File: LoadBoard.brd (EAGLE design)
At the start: 100 x 100 mm, 76 parts, among them IC1 7805TV, IC2 LM358D, IC3 MCP23S17SO, Q1 IRFZ44N, Q2 16MHz, T1 BC817, U1 ATMEGA328P_TQFP, U2 MAX232SOIC16

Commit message: routed first version of the board
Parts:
- added ENCODER, JP3: (no value), SparkFun-Connectors:MOLEX-1X4
- added FAN_CTRL, VLOAD_ATT: TPB1,27, testpad:B1,27
- added H5, H6: 3MM, holes:3,0-PAD
- added KK3: SK104-PAD, heatsink:SK104-PAD
- added LED1, LED2: (no value), led:Q62902-B155
- added Q3: IRFZ44N, OwnStuff:TO-220-V
- added R14, R15, R16: 100, rcl:R1206
- added R17, R18: 4k7, rcl:M1206
- added RST_EN: (no value), pinhead:1X02
- added U$7, U$8: DS18B20, OwnStuff:TO-92
- KK1: value SK129 -> SK104-PAD; device heatsink:SK129-HOLE -> heatsink:SK104-PAD
- moved U$4 60.9 mm to (62.2, 38.1), turned to 270 degrees
- moved S1 58.3 mm to (41.9, 88.6)
- moved T1 54.3 mm to (62.2, 43.2), turned to 270 degrees
- moved R6 51.2 mm to (55.9, 43.2), turned to 0 degrees
- moved FAN 48.7 mm to (62.2, 47.0), turned to 90 degrees
- moved D1 45.4 mm to (55.9, 48.3), turned to 270 degrees
- moved KK1 44.9 mm to (91.4, 68.6), turned to 270 degrees
- moved Q1 38.4 mm to (86.4, 68.6), turned to 270 degrees
- moved R3 33.2 mm to (80.0, 72.4), turned to 0 degrees
- moved U$5 32.8 mm to (11.4, 48.3)
- moved R5 30.4 mm to (74.9, 48.9), turned to 90 degrees
- moved R13 30.2 mm to (80.0, 68.6), turned to 180 degrees
- moved Q2 28.0 mm to (41.9, 41.9)
- moved R12 27.9 mm to (80.0, 64.8), turned to 0 degrees
- moved C6 26.7 mm to (48.3, 48.3)
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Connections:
- new net GNDIO: JP3.1, S1.C, S1.SW-
- new net LED1: R14.1, U1.27
- new net LED2: R15.1, U1.28
- new net N$43: LED1.A, R14.2
- new net N$44: LED2.A, R15.2
- new net N$45: JP3.4, S1.SW+
- new net N$46: JP3.3, S1.A
- new net N$47: Q3.1, R16.2
- new net N$49: JP3.2, S1.B
- new net RST_EN: C12.2, RST_EN.1
- new net TH1: R18.2, U$7.2, U1.23
- new net TH2: R17.2, U$8.2, U1.24
- net +12V: now also FAN.2; no longer FAN.1
- net BTN_A: now also U1.2; no longer U1.1
- net BTN_B: now also U1.1; no longer U1.2
- net ENC_A: now also ENCODER.3; no longer S1.A
- net ENC_B: now also ENCODER.2; no longer S1.B
- net ENC_BTN: now also ENCODER.4; no longer S1.SW+
- net FAN: now also FAN_CTRL.TP
- net GND: now also ENCODER.1, LED1.K, LED2.K, U$7.1, U$8.1; no longer S1.C, S1.SW-
- net LOAD+: now also Q3.2
- net N$10: now also R16.1
- net N$12: now also DTR_IN.TP; no longer RX_IN.TP
- net N$13: now also RX_IN.TP; no longer DTR_IN.TP
- net N$26: now also PWR_SWITCH.2; no longer PWR_SWITCH.1
- net N$35: now also U$6.CS2; no longer U$6.DI
- net N$36: now also U$6.CS1; no longer U$6.RW
- net N$38: now also U$6.RW; no longer U$6.CS1
- net N$39: now also U$6.DI; no longer U$6.CS2
- net N$41: now also PWR_SWITCH.1; no longer PWR_SWITCH.2
- net N$5: now also FAN.1; no longer FAN.2
- net N$7: now also RST_EN.2; no longer C12.2
- net VCC: now also R17.1, R18.1, U$7.3, U$8.3
- net VLOAD_ATT: now also VLOAD_ATT.TP
- net VLOAD_DROP: now also Q3.3, U1.25
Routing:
- net VCC: track 0.00 -> 233.1 mm, vias 0 -> 7
- net VLOAD_DROP: track 0.00 -> 161.5 mm, vias 0 -> 1
- net +12V: track 0.00 -> 123.2 mm, vias 0 -> 2
- net TH1: track 0.00 -> 120.8 mm, vias 0 -> 3
- net TH2: track 0.00 -> 115.6 mm, vias 0 -> 2
- net MOSI: track 0.00 -> 107.8 mm, vias 0 -> 3
- net SCK: track 0.00 -> 97.2 mm, vias 0 -> 2
- net VLOAD_ATT: track 0.00 -> 95.8 mm, vias 0 -> 2
- net RST: track 0.00 -> 92.4 mm, vias 0 -> 2
- net BTN_B: track 0.00 -> 92.0 mm, vias 0 -> 2
- net LOAD+: track 0.00 -> 87.3 mm
- net BTN_A: track 0.00 -> 87.0 mm, vias 0 -> 2
- net LED1: track 0.00 -> 72.9 mm, vias 0 -> 2
- net N$10: track 0.00 -> 72.1 mm
- net CS1: track 0.00 -> 68.1 mm, vias 0 -> 2
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- added copper zone on layer 1, net GNDIO
- added copper zone on layer 16, net GNDIO
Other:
- board size 100 x 100 mm -> 99 x 99 mm

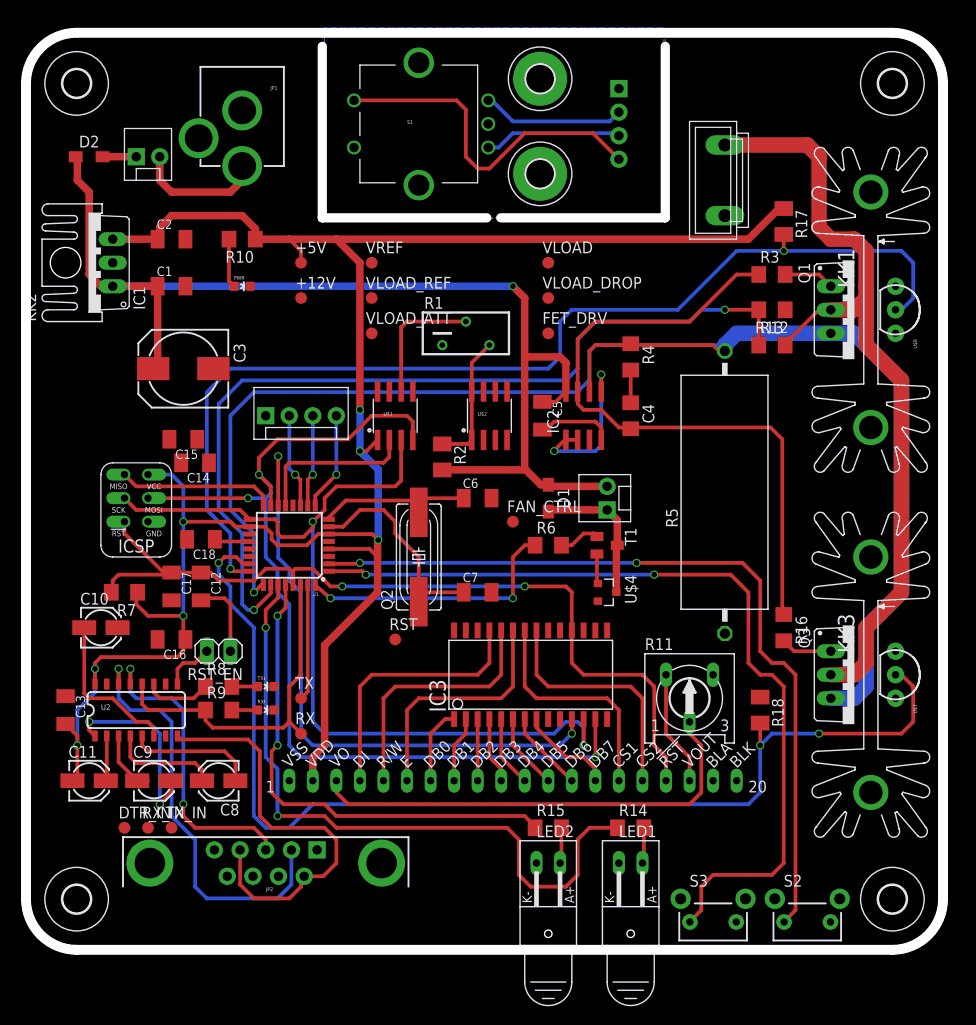
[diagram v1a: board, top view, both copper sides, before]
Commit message: Routed more of the Board, added an optional LM2569 Module
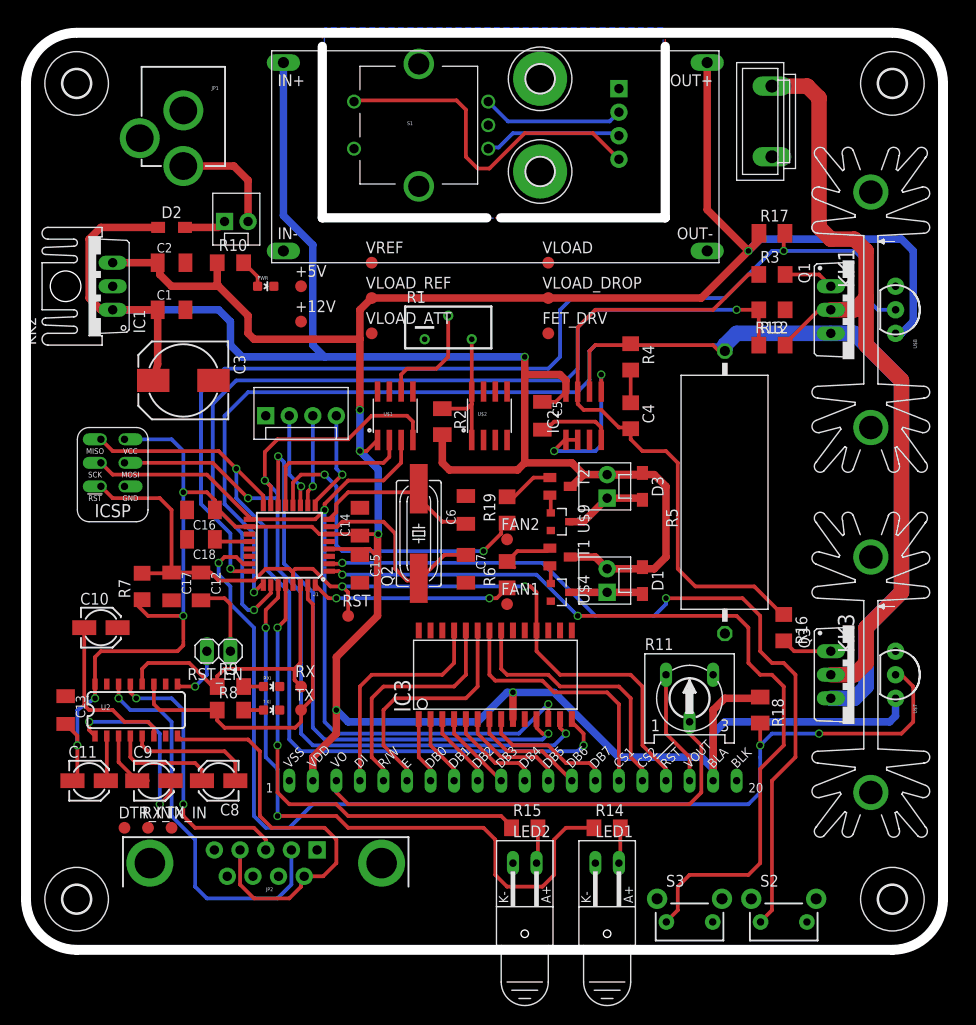
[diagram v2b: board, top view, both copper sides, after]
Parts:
- removed FAN: (no value), SparkFun-Connectors:MOLEX-1X2
- removed FAN_CTRL: TPB1,27, testpad:B1,27
- added D3: BAS16J, diode:SOD323-W
- added FAN1, FAN2: TPB1,27, testpad:B1,27
- added FAN1_CONN, FAN2_CONN: (no value), SparkFun-Connectors:MOLEX-1X2
- added R19: 100, rcl:R1206
- added T2: BC817, transistor:SOT23-BEC
- added U$10: LM2569, OwnStuff:LM2596
- added U$9: IRLML2502, GeekAmmo:SOT23-3
- moved C15 23.6 mm to (35.6, 40.6), turned to 270 degrees
- moved C14 18.9 mm to (35.6, 45.7), turned to 90 degrees
- moved C16 14.3 mm to (18.4, 47.0)
- moved D1 13.5 mm to (66.0, 39.4)
- moved PWR_SWITCH 11.8 mm to (21.0, 78.1)
- moved D2 11.7 mm to (15.2, 77.5)
- moved U$3 8.13 mm to (80.0, 88.9)
- moved JP1 6.35 mm to (16.5, 97.8)
- moved RST 5.68 mm to (34.3, 35.6)
- moved R6 5.46 mm to (51.4, 40.0), turned to 90 degrees
- moved T1 5.24 mm to (57.1, 41.9)
- moved RX 5.08 mm to (29.2, 27.9)
- moved U$4 5.08 mm to (57.1, 38.1)
- moved U$5 4.58 mm to (8.89, 52.1)
- moved IC3 3.81 mm to (49.5, 29.2)
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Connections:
- removed net FAN: FAN_CTRL.TP, R6.1, U1.32
- new net FAN1: FAN1.TP, R6.1, U1.32
- new net FAN2: FAN2.TP, R19.1, U1.12
- new net N$42: T2.E, U$9.1
- new net N$48: R19.2, T2.B
- new net N$50: D3.A, FAN2_CONN.1, U$9.3
- net +12V: now also D3.C, FAN1_CONN.2, FAN2_CONN.2, T1.C, T2.C, U$10.IN+; no longer FAN.2
- net GND: now also U$10.IN-, U$10.OUT-, U$9.2
- net N$5: now also FAN1_CONN.1; no longer FAN.1, T1.C
- net VCC: now also U$10.OUT+
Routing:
- net VCC: track 233.1 -> 373.1 mm, vias 7 -> 10
- net MISO: track 17.0 -> 88.6 mm, vias 0 -> 2
- net +12V: track 123.2 -> 187.0 mm, vias 2 -> 1
- net FAN2: track 0.00 -> 34.8 mm, vias 0 -> 2
- net FAN: track 29.2 -> 0.00 mm, vias 2 -> 0
- net FAN1: track 0.00 -> 22.0 mm, vias 0 -> 2
- net TX: track 19.8 -> 35.5 mm
- net N$50: track 0.00 -> 9.02 mm
- net N$5: track 15.8 -> 7.96 mm
- net SCK: track 97.2 -> 90.8 mm
- net N$48: track 0.00 -> 5.60 mm
- net RX: track 37.1 -> 32.3 mm
- net RST: track 92.4 -> 97.1 mm
- net N$34: track 10.4 -> 14.6 mm
- net N$39: track 28.7 -> 24.9 mm
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
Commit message: worked on silkscreen for passives
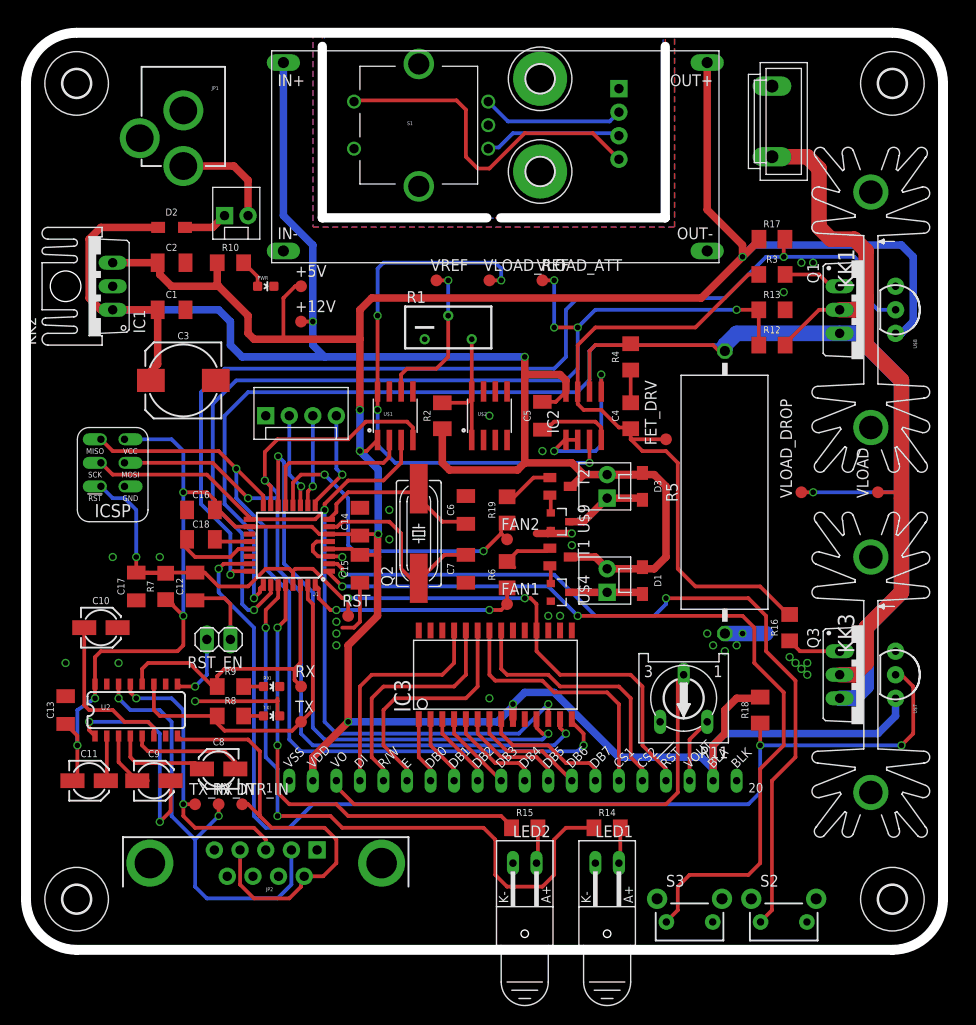
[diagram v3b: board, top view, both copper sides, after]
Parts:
- C3: value 24µ -> 100µ; device rcl:150CLZ-0810 -> rcl:175TMP-0808
- moved VLOAD 43.3 mm to (91.4, 48.9), turned to 90 degrees
- moved VLOAD_DROP 34.4 mm to (83.2, 48.9), turned to 90 degrees
- moved VLOAD_ATT 19.3 mm to (55.2, 71.8)
- moved FET_DRV 17.1 mm to (68.6, 54.6), turned to 90 degrees
- moved DTR_IN 13.0 mm to (22.9, 15.2)
- moved VLOAD_REF 12.8 mm to (49.5, 71.8)
- moved RX_IN 8.03 mm to (20.3, 15.2)
- moved VREF 7.24 mm to (43.8, 71.8)
- moved C17 3.81 mm to (11.4, 38.7)
- moved TX_IN 3.59 mm to (17.8, 15.2)
- moved R7 2.54 mm to (14.6, 38.7)
- moved RST_EN 1.27 mm to (20.3, 33.0)
- moved C8 1.27 mm to (20.3, 19.1)
- moved TX 1.27 mm to (29.2, 24.1)
- moved Q1 0.95 mm to (87.3, 68.6)
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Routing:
- net VLOAD_REF: track 0.00 -> 61.6 mm, vias 0 -> 4
- net GND: track 9.08 -> 49.9 mm, vias 0 -> 31
- net VLOAD_DROP: track 162.4 -> 173.4 mm, vias 1 -> 2
- net VLOAD_ATT: track 97.4 -> 106.3 mm, vias 2 -> 5
- net LOAD+: track 88.6 -> 82.8 mm
- net N$25: track 12.5 -> 7.14 mm
- net N$2: track 12.1 -> 17.2 mm, vias 0 -> 1
- net N$13: track 42.4 -> 47.3 mm, vias 1 -> 2
- net N$10: track 69.7 -> 73.8 mm
- net N$16: track 20.6 -> 24.4 mm
- net FAN1: track 22.0 -> 24.4 mm
- net N$12: track 45.2 -> 47.6 mm
- net +12V: track 187.0 -> 189.2 mm, vias 1 -> 2
- net N$24: track 49.8 -> 51.7 mm
- net N$7: track 6.35 -> 7.62 mm
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- added copper zone on layer 1, net GND
- added copper zone on layer 16, net GND

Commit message: added silkscreen information to bottom
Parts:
- added IC6: MCP4921, OwnStuff:SO-8
- added IC7: TL431CD, OwnStuff:SO-8
- added LED3: (no value), led:Q62902-B155
- added R20: 100, rcl:R1206
- Q1, Q3: value IRFZ44N -> IRF3710
- U$1: value MCP4921 -> (none); device OwnStuff:SO-8 -> OwnStuff:LOGO-SILKSCREEN
- U$10: value LM2569 -> LM2569NO_OUTLINE; device OwnStuff:LM2596 -> OwnStuff:LM2596_NO_OUTLINE
- U$2: value TL431CD -> (none); device OwnStuff:SO-8 -> SparkFun-Aesthetics:OSHW-LOGO-L
- moved U$1 41.0 mm to (80.0, 51.4), flipped to the bottom
- moved U$2 19.7 mm to (68.6, 52.1), flipped to the bottom
- moved R14 15.3 mm to (47.0, 12.1)
- moved LED1 15.2 mm to (47.0, 1.27)
- moved U$10 10.2 mm to (50.2, 85.1)
- moved FAN2 2.84 mm to (48.9, 42.5)
- moved FAN1 2.62 mm to (48.9, 36.2)
- moved C7 1.42 mm to (46.4, 39.4)
- moved R15 1.42 mm to (54.6, 12.1)
- moved DTR_IN 1.27 mm to (24.1, 15.2)
- moved LED2 1.27 mm to (54.6, 1.27)
- moved C6 0.64 mm to (46.4, 47.0)
- moved R6 0.64 mm to (51.4, 39.4)
- moved C8 0.63 mm to (20.3, 19.7)
- moved R2 0.63 mm to (45.1, 57.1)
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- renumbered ENCODER to JP4, PWR to LED4, RST_EN to JP5, RXI to LED5, TXI to LED6, U$4 to U4, U$7 to IC8, U$8 to IC9, U$9 to U9, U1 to IC4, U2 to IC5
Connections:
- new net N$51: LED3.A, R20.2
- net CS2: now also IC6.2; no longer U$1.2
- net GND: now also IC6.5, IC6.7, IC7.2, IC7.3, IC7.6, IC7.7, LED3.K; no longer U$1.5, U$1.7, U$2.2, U$2.3, U$2.6, U$2.7
- net MOSI: now also IC6.4; no longer U$1.4
- net N$1: now also IC7.1, IC7.8; no longer U$2.1, U$2.8
- net N$2: now also IC6.6; no longer U$1.6
- net SCK: now also IC6.3; no longer U$1.3
- net VCC: now also IC6.1, R20.1; no longer U$1.1
- net VLOAD_REF: now also IC6.8; no longer U$1.8
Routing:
- net LED1: track 70.4 -> 45.7 mm
- net VCC: track 372.6 -> 388.5 mm
- net N$51: track 0.00 -> 6.28 mm
- net +12V: track 189.2 -> 185.5 mm
- net N$37: track 25.9 -> 22.3 mm
- net N$38: track 25.4 -> 22.9 mm
- net TH2: track 114.4 -> 116.8 mm
- net CS1: track 64.8 -> 62.6 mm
- net MISO: track 88.6 -> 86.8 mm
- net N$12: track 47.6 -> 46.1 mm
- net N$36: track 28.3 -> 26.8 mm
- net N$39: track 24.9 -> 23.4 mm
- net N$35: track 28.8 -> 27.4 mm
- net RST: track 96.4 -> 94.9 mm
- net LED2: track 49.7 -> 51.1 mm
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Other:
- board text added: "+"
- board text added: "0R1 Shunt Resistor 5W"
- board text added: "10V"
- board text added: "12V"
- board text added: "12V IN"
- board text added: "2.5A"
- board text added: "20V"
- board text added: "50W"
- board text added: "5A"
- board text added: "ENCODER"
- board text added: "FAN 1"
- board text added: "FAN 2"
- board text added: "Heat Shutdown"
- board text added: "I SET"
- board text added: "LOAD INPUT"
- board text added: "Load Enable"
- board text added: "MAX232"
- board text added: "MCP23S17"
- board text added: "Maximum Ratings:"
- board text added: "Mega 328"
- board text added: "P MAX"
- board text added: "POWER SWITCH"
- board text added: "Power"
- board text added: "RS232"
- board text added: "Reset on DTR"
- board text added: "Smart Dummy Load"
- board text added: "U IN"
- board text added: "by nupo-artworks.de"
